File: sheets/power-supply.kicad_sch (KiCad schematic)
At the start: 7 parts, among them J1 Power Input, SW1 POWER SWITCH

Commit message: add MCU + output
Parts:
- renumbered D3 to D2, D2 to D3
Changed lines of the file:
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@@
 		(dnp no)
 		(fields_autoplaced yes)
-		(property "Reference" "D2"
+		(property "Reference" "D3"
 			(at 93.98 36.8299 90)
 			(effects
@@
 			(project "esp32-didatic-kit"
 				(path "/f57920a5-fee7-4fe5-a133-e8b36941a5a6/68eb6d36-2b61-4a79-8b9e-43cc2ec0c3c5"
-					(reference "D2")
+					(reference "D3")
 					(unit 1)
 				)
@@
 		(dnp no)
 		(fields_autoplaced yes)
-		(property "Reference" "#PWR012"
+		(property "Reference" "#PWR07"
 			(at 229.87 54.61 0)
 			(effects
@@
 			(project ""
 				(path "/f57920a5-fee7-4fe5-a133-e8b36941a5a6/68eb6d36-2b61-4a79-8b9e-43cc2ec0c3c5"
-					(reference "#PWR012")
+					(reference "#PWR07")
 					(unit 1)
 				)
@@
 		(dnp no)
 		(fields_autoplaced yes)
-		(property "Reference" "#PWR015"
+		(property "Reference" "#PWR03"
 			(at 123.19 118.11 0)
 			(effects
@@
 			(project "esp32-didatic-kit"
 				(path "/f57920a5-fee7-4fe5-a133-e8b36941a5a6/68eb6d36-2b61-4a79-8b9e-43cc2ec0c3c5"
-					(reference "#PWR015")
+					(reference "#PWR03")
 					(unit 1)
 				)
@@
 		(dnp no)
 		(fields_autoplaced yes)
-		(property "Reference" "#PWR010"
+		(property "Reference" "#PWR05"
 			(at 228.6 81.28 0)
 			(effects
@@
 			(project ""
 				(path "/f57920a5-fee7-4fe5-a133-e8b36941a5a6/68eb6d36-2b61-4a79-8b9e-43cc2ec0c3c5"
-					(reference "#PWR010")
+					(reference "#PWR05")
 					(unit 1)
 				)
@@
 		(dnp no)
 		(fields_autoplaced yes)
-		(property "Reference" "D3"
+		(property "Reference" "D2"
 			(at 81.28 52.0699 90)
 			(effects
@@
 			(project "esp32-didatic-kit"
 				(path "/f57920a5-fee7-4fe5-a133-e8b36941a5a6/68eb6d36-2b61-4a79-8b9e-43cc2ec0c3c5"
-					(reference "D3")
+					(reference "D2")
 					(unit 1)
 				)
@@
 		(dnp no)
 		(fields_autoplaced yes)
-		(property "Reference" "#PWR011"
+		(property "Reference" "#PWR06"
 			(at 229.87 35.56 0)
 			(effects
@@
 			(project ""
 				(path "/f57920a5-fee7-4fe5-a133-e8b36941a5a6/68eb6d36-2b61-4a79-8b9e-43cc2ec0c3c5"
-					(reference "#PWR011")
+					(reference "#PWR06")
 					(unit 1)
 				)
@@
 		(dnp no)
 		(fields_autoplaced yes)
-		(property "Reference" "#PWR017"
+		(property "Reference" "#PWR04"
 			(at 173.99 118.11 0)
 			(effects
@@
 			(project "esp32-didatic-kit"
 				(path "/f57920a5-fee7-4fe5-a133-e8b36941a5a6/68eb6d36-2b61-4a79-8b9e-43cc2ec0c3c5"
-					(reference "#PWR017")
+					(reference "#PWR04")
 					(unit 1)
 				)
@@
 		(dnp no)
 		(fields_autoplaced yes)
-		(property "Reference" "#PWR018"
+		(property "Reference" "#PWR08"
 			(at 233.68 120.65 0)
 			(effects
@@
 			(project "esp32-didatic-kit"
 				(path "/f57920a5-fee7-4fe5-a133-e8b36941a5a6/68eb6d36-2b61-4a79-8b9e-43cc2ec0c3c5"
-					(reference "#PWR018")
+					(reference "#PWR08")
 					(unit 1)
 				)
@@
 		(dnp no)
 		(fields_autoplaced yes)
-		(property "Reference" "#PWR013"
+		(property "Reference" "#PWR02"
 			(at 119.38 82.55 0)
 			(effects
@@
 			(project ""
 				(path "/f57920a5-fee7-4fe5-a133-e8b36941a5a6/68eb6d36-2b61-4a79-8b9e-43cc2ec0c3c5"
-					(reference "#PWR013")
-					(unit 1)
-				)
+					(reference "#PWR02")
+					(unit 1)
+				)

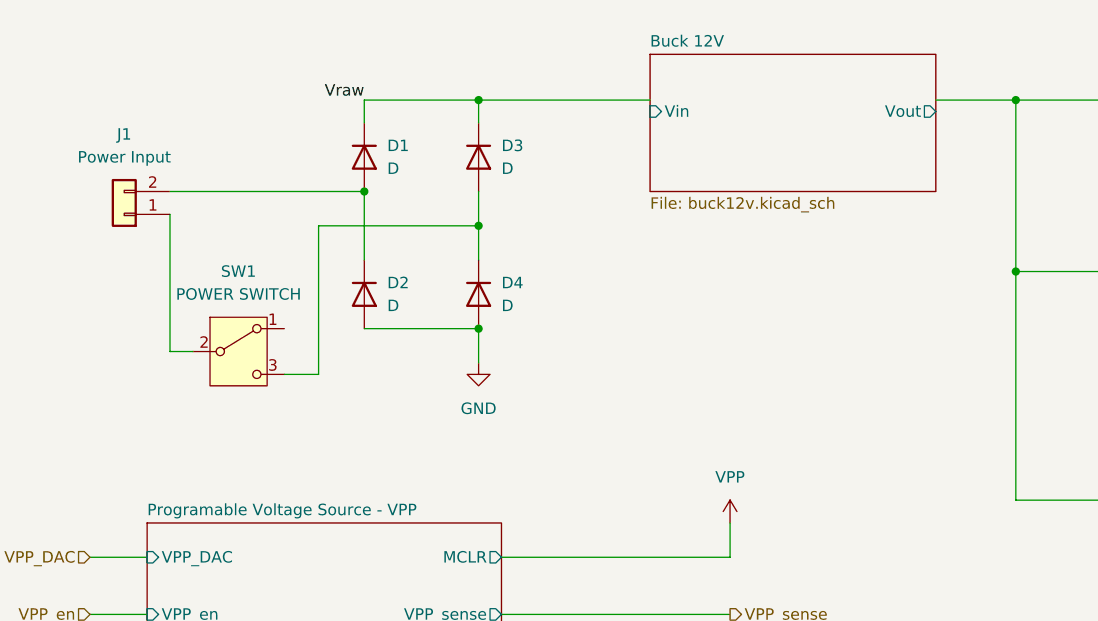
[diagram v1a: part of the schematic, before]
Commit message: Updated MCU to MCU module + set SMD comp. footprints
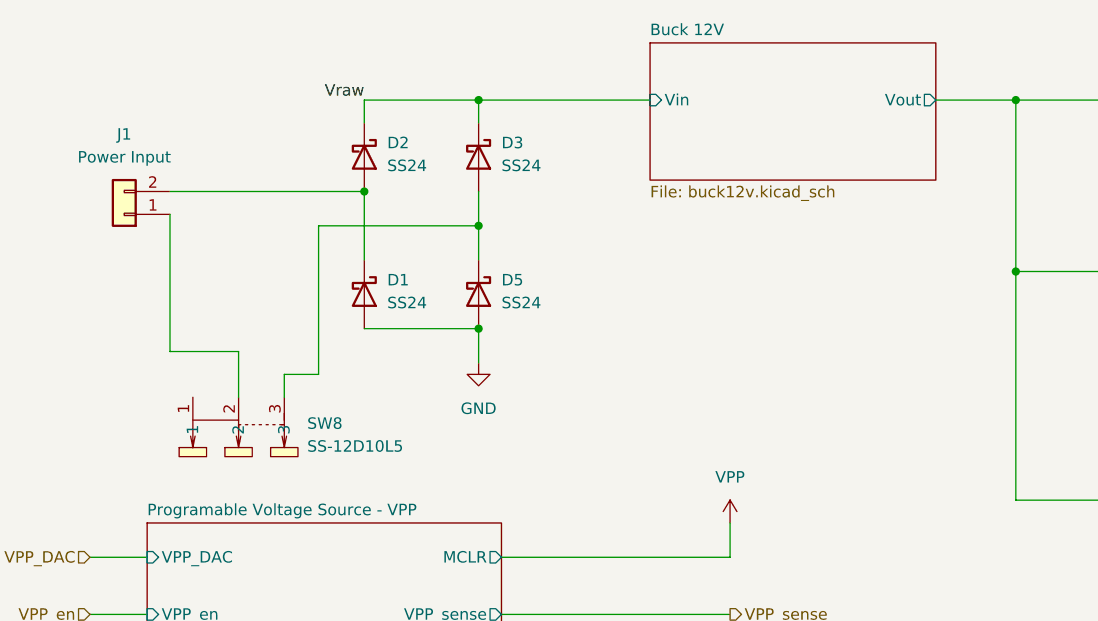
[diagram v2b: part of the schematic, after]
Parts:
- removed D1, D2, D3, D4: D, symbol Device:D
- removed SW1: POWER SWITCH, symbol Switch:SW_SPDT
- added D1, D2, D3, D5: SS24, Diode_SMD:D_SMA, symbol Diode:SS24
- added SW8: SS-12D10L5, Connectors:SW-TH_SS-12D10L5, symbol Connectors:SS-12D10L5
- J1: footprint (none) -> TerminalBlock_Phoenix:TerminalBlock_Phoenix_MKDS-1,5-2-5.08_1x02_P5.08mm_Horizontal
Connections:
- net GND: now also D1.2 (A), D5.2 (A)
- net Vraw: now also D2.1 (K), D3.1 (K)
- net at J1.1 (Pin_1): now also SW8.2
- net at J1.2 (Pin_2): now also D1.1 (K), D2.2 (A)
- new net: D3.2 (A), D5.1 (K), SW8.3
